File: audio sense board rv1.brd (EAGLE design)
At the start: 132.1 x 26.7 mm, 33 parts, among them IC2 TSOP38238, J1 PJRAN1X1U01X, J2 PJRAN1X1U01X, Q1 2N3904, Q2 2N3904

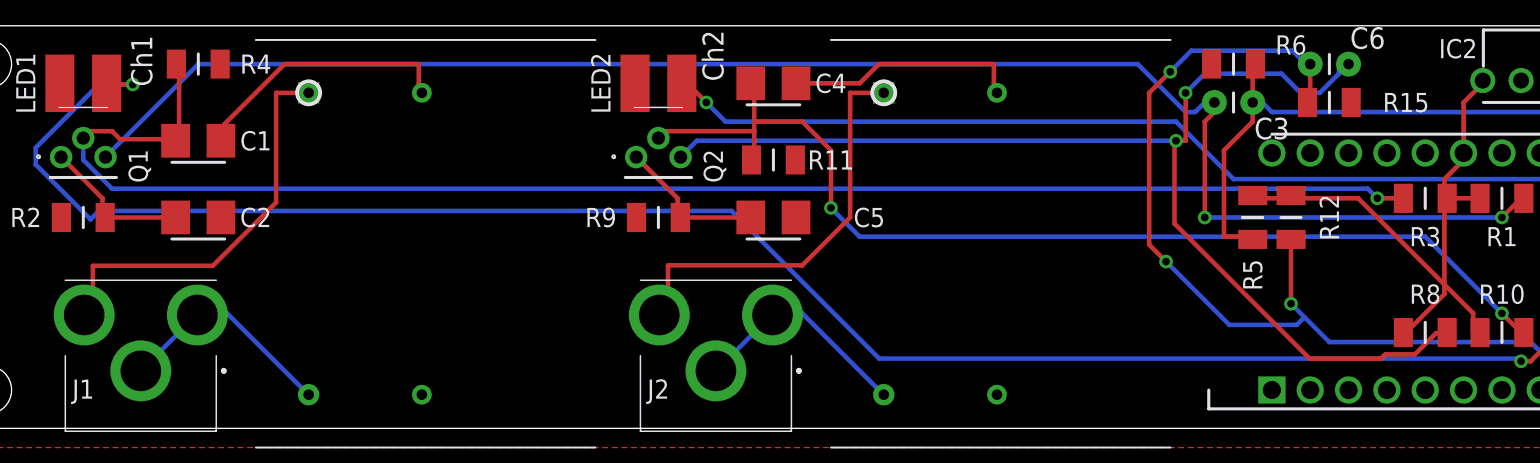
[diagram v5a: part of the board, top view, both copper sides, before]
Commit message: increase clearance on transformer and C2 pad
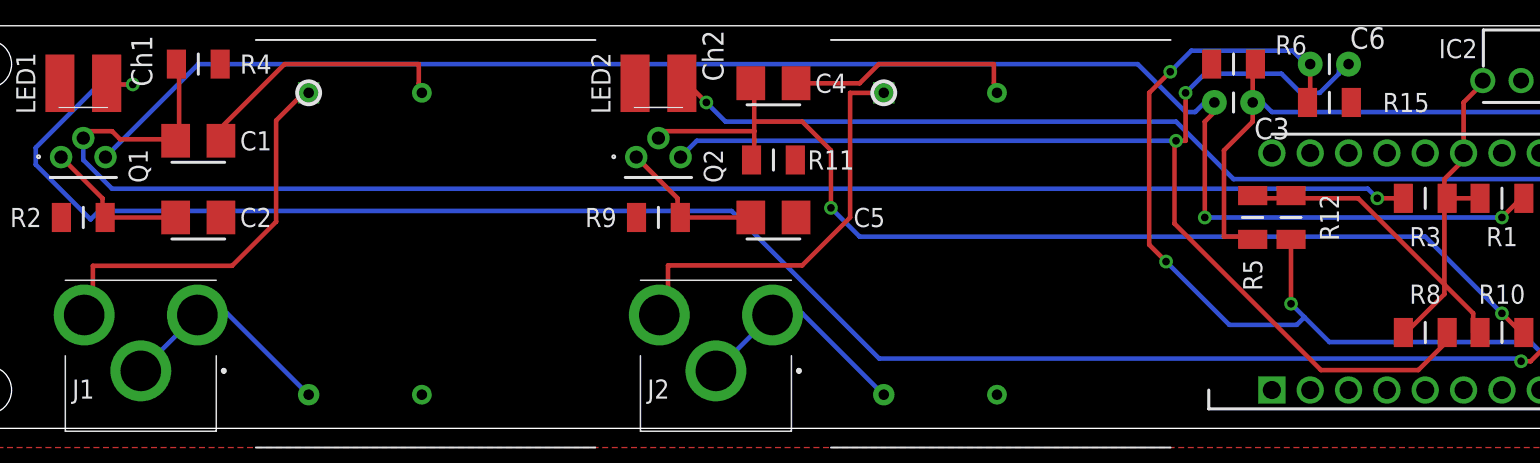
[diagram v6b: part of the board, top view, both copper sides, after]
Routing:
- net N$8: track 78.1 -> 79.1 mm
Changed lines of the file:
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@@
 <contactref element="J1" pad="2"/>
 <contactref element="L1" pad="1"/>
-<wire x1="21.6662" y1="22.225" x2="23.495" y2="22.225" width="0.3048" layer="1"/>
+<wire x1="21.6662" y1="20.3962" x2="23.495" y2="22.225" width="0.3048" layer="1"/>
 <wire x1="9.525" y1="7.62" x2="9.525" y2="10.7696" width="0.3048" layer="1"/>
 <wire x1="23.495" y1="22.225" x2="23.82" y2="22.23" width="0.3048" layer="1"/>
 <wire x1="9.525" y1="7.62" x2="8.95" y2="7.51" width="0.3048" layer="1"/>
-<wire x1="21.6662" y1="14.9606" x2="21.6662" y2="22.225" width="0.3048" layer="1"/>
-<wire x1="17.4752" y1="10.7696" x2="21.6662" y2="14.9606" width="0.3048" layer="1"/>
-<wire x1="9.525" y1="10.7696" x2="17.4752" y2="10.7696" width="0.3048" layer="1"/>
+<wire x1="21.6662" y1="13.6906" x2="21.6662" y2="20.3962" width="0.3048" layer="1"/>
+<wire x1="18.7452" y1="10.7696" x2="21.6662" y2="13.6906" width="0.3048" layer="1"/>
+<wire x1="9.525" y1="10.7696" x2="18.7452" y2="10.7696" width="0.3048" layer="1"/>
 </signal>
 <signal name="N$17">
@@
 <via x="81.28" y="19.05" extent="1-16" drill="0.508"/>
 <wire x1="89.535" y1="22.225" x2="90.805" y2="22.225" width="0.3048" layer="16"/>
-<wire x1="98.5012" y1="6.2992" x2="99.06" y2="6.2992" width="0.3048" layer="1"/>
-<wire x1="97.1042" y1="4.9022" x2="98.5012" y2="6.2992" width="0.3048" layer="1"/>
-<wire x1="95.1484" y1="4.9022" x2="97.1042" y2="4.9022" width="0.3048" layer="1"/>
-<wire x1="94.869" y1="4.6228" x2="95.1484" y2="4.9022" width="0.3048" layer="1"/>
-<wire x1="90.1192" y1="4.6228" x2="94.869" y2="4.6228" width="0.3048" layer="1"/>
-<wire x1="81.1784" y1="13.5636" x2="90.1192" y2="4.6228" width="0.3048" layer="1"/>
+<wire x1="99.24" y1="6.35" x2="99.24" y2="5.768" width="0.3048" layer="1"/>
+<wire x1="99.24" y1="5.768" x2="97.3328" y2="3.8608" width="0.3048" layer="1"/>
+<wire x1="90.8812" y1="3.8608" x2="97.3328" y2="3.8608" width="0.3048" layer="1"/>
+<wire x1="81.1784" y1="13.5636" x2="90.8812" y2="3.8608" width="0.3048" layer="1"/>
 <wire x1="81.1784" y1="18.8722" x2="81.1784" y2="13.5636" width="0.3048" layer="1"/>
-<wire x1="99.06" y1="6.2992" x2="99.24" y2="6.35" width="0.3048" layer="1"/>
 <wire x1="81.1784" y1="18.8722" x2="81.28" y2="19.05" width="0.3048" layer="1"/>
 </signal>
